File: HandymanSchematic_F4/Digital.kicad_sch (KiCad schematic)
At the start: 45 parts, among them J1 SWD Header, J2 Footswitch, J3 TunerIn, J4 TuneThru, J5 GateIn, J6 GateOut, J7 PowerJack, Q2 2N7002, Q3 2N7002, SW1 RST, SW2 BYP, U1 SH1106, U3 STM32F411RETx, U4 AMS1117, Y1 16MHz

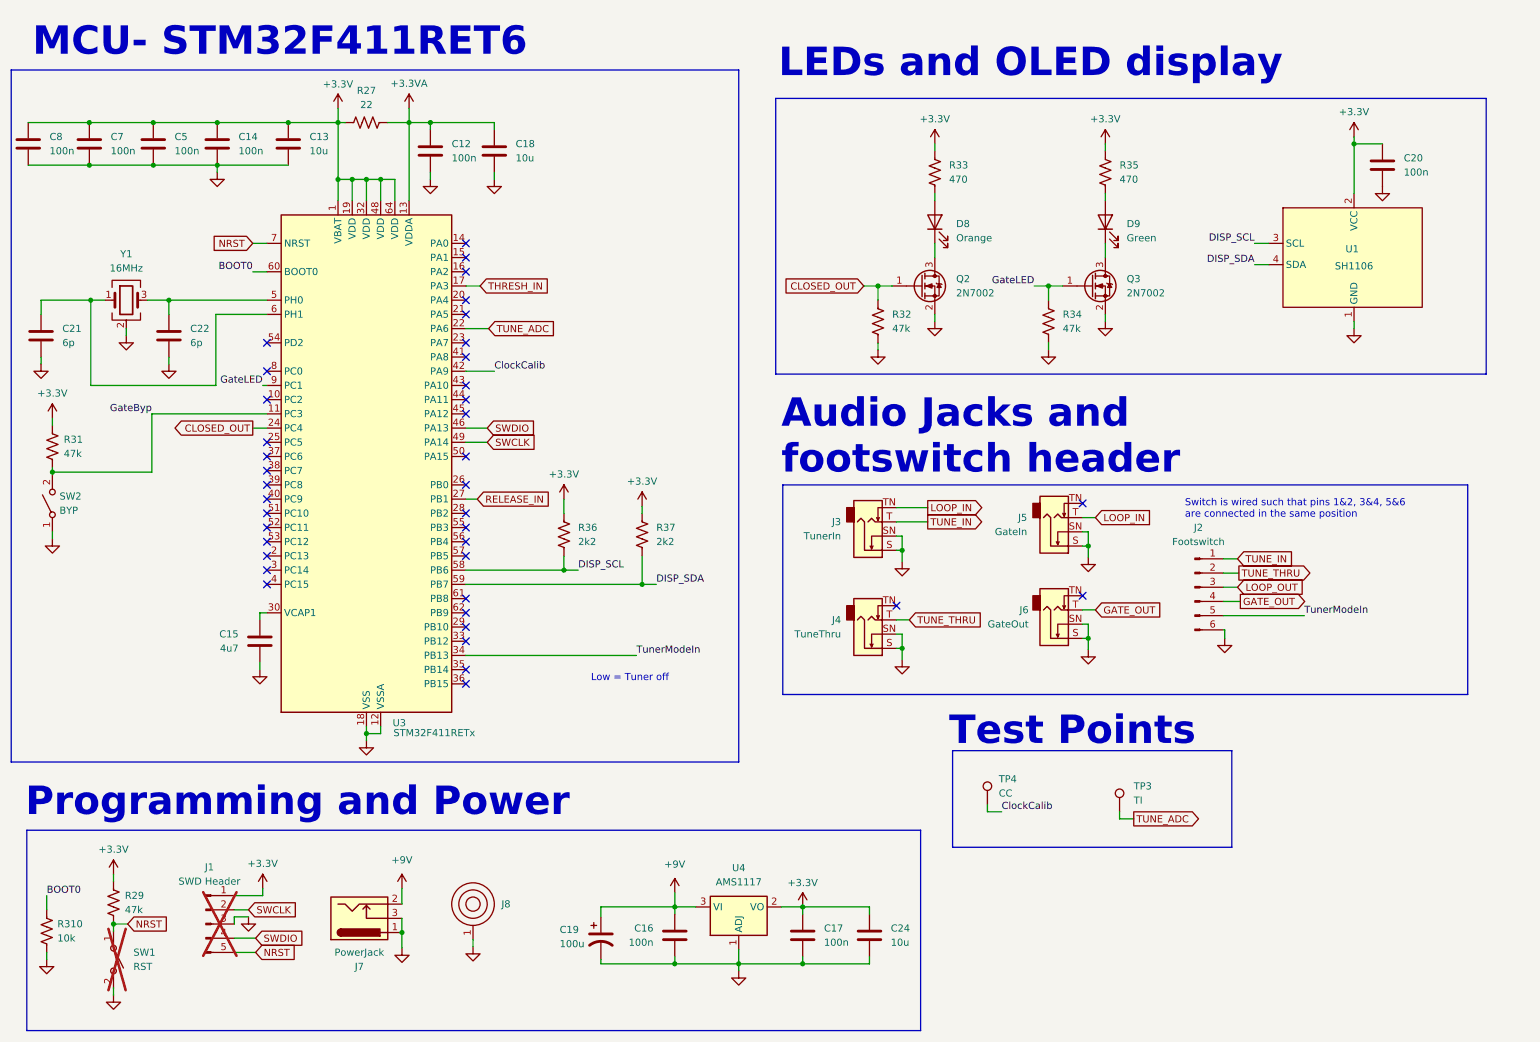
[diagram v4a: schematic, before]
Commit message: moved to front, routing and DRC done
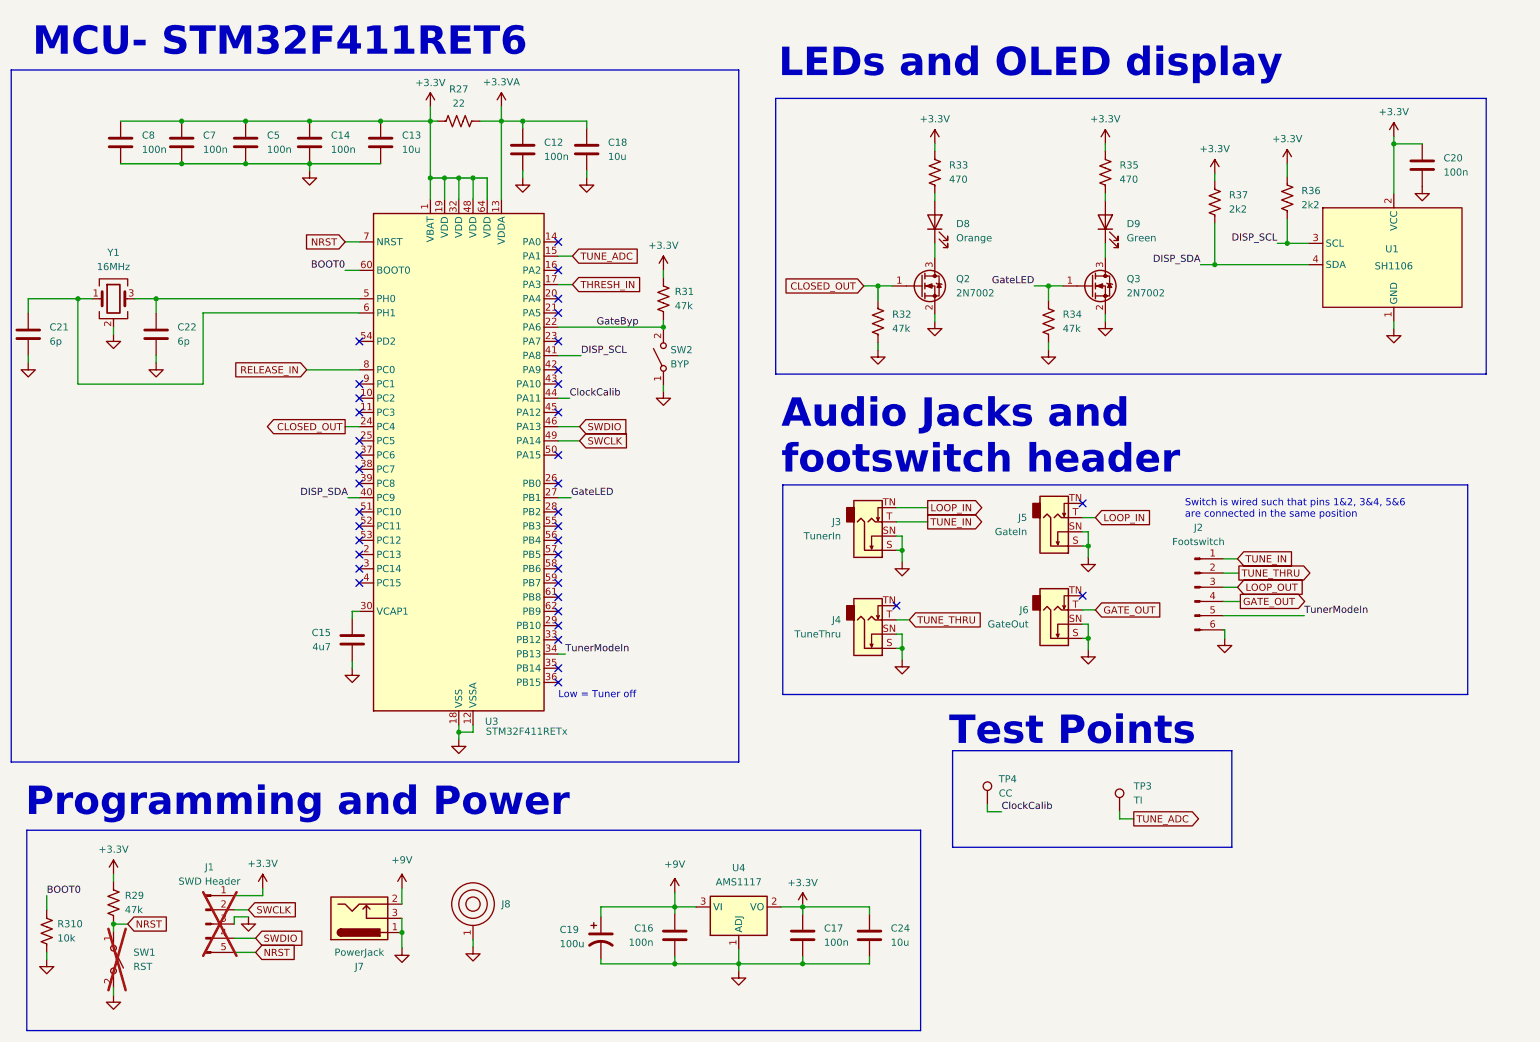
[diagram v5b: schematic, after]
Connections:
- net ClockCalib: now also U3.44 (PA11); no longer U3.42 (PA9)
- net DISP_SCL: now also U3.41 (PA8); no longer U3.58 (PB6)
- net DISP_SDA: now also U3.40 (PC9); no longer U3.59 (PB7)
- net GateByp: now also U3.22 (PA6); no longer U3.11 (PC3)
- net GateLED: now also U3.27 (PB1); no longer U3.9 (PC1)
- net RELEASE_IN: now also U3.8 (PC0); no longer U3.27 (PB1)
- net TUNE_ADC: now also U3.15 (PA1); no longer U3.22 (PA6)
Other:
- moved on the sheet: C12, C13, C14, C15, C18, C20, C21, C22, C5, C7, C8, R27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

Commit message: noise schematic tweaks
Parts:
- added C26: 470u, Capacitor_THT:CP_Radial_D6.3mm_P2.50mm, symbol Device:C_Polarized_US
- added R40: 22, Resistor_SMD:R_0805_2012Metric, symbol Device:R_US
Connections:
- net +9V: now also R40.2
- net GND: now also C26.2
- new net +9VA: C26.1, R40.1
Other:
- moved on the sheet: C16, C17, C19, C24, J1, J7, J8, U4

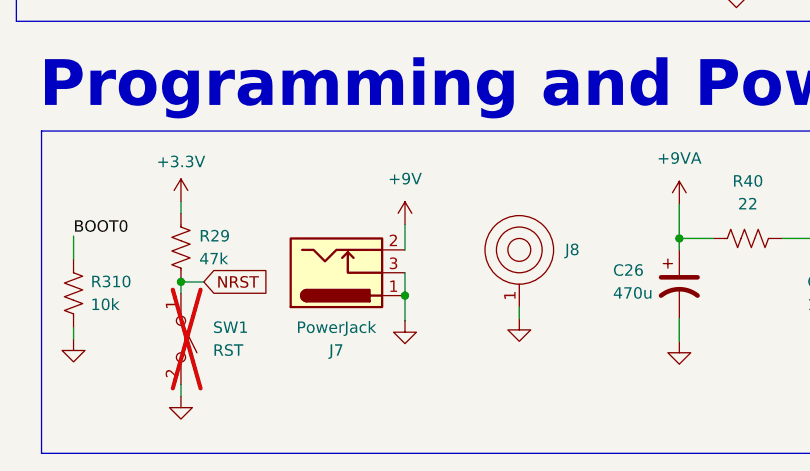
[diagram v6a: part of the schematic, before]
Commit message: added anti-ringing caps, widened jack spacing a bit
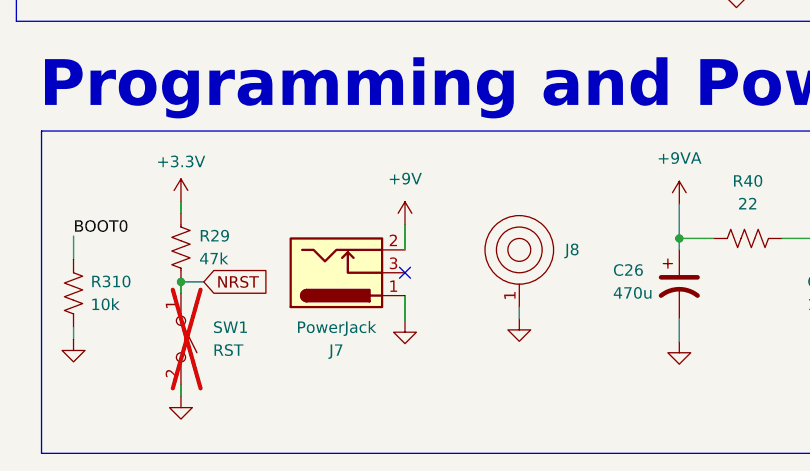
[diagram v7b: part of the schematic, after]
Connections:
- net GND: no longer J7.3
- no-connect marks 39 -> 40
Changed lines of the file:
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@@
-	)
-	(junction
-		(at 55.88 176.53)
-		(diameter 0)
-		(color 0 0 0 0)
 	)
 	(junction
@@
 	(no_connect
 		(at 110.49 111.506)
+	)
+	(no_connect
+		(at 55.88 173.99)
 	)
 	(no_connect
@@
 		)
 		(stroke
-			(width 0)
-			(type default)
-		)
-	)
-	(wire
-		(pts
-			(xy 55.88 173.99) (xy 55.88 176.53)
-		)
-		(stroke
